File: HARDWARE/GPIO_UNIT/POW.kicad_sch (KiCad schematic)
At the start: 20 parts, among them J401 Screw_Terminal_01x02, U301 L78L05_SOT89, U901 MT2499A

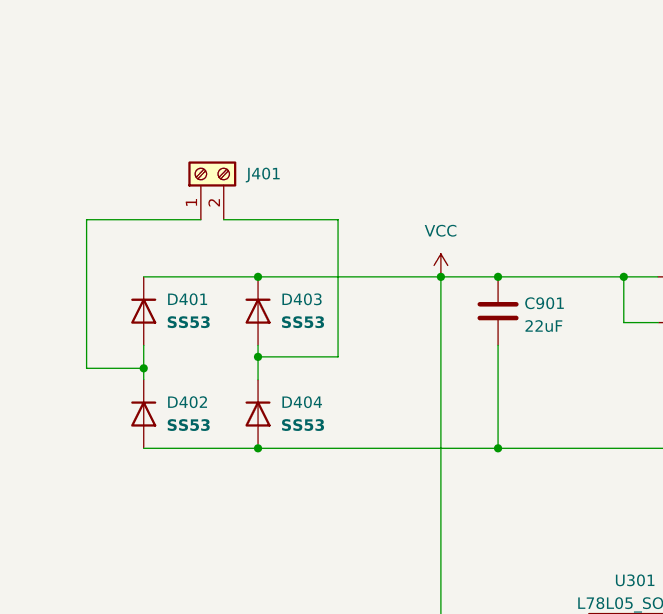
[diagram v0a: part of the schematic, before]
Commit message: added GPIO UNIT board. To be renamed Jack Of All trades
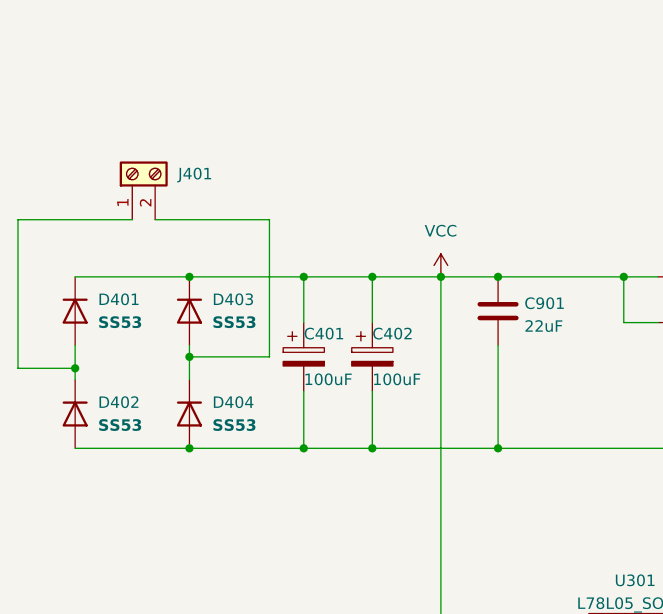
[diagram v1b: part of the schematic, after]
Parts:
- added C401, C402: 100uF, Capacitor_SMD:CP_Elec_6.3x5.8, symbol Device:C_Polarized
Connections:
- net GND: now also C401.2, C402.2
- net VCC: now also C401.1, C402.1
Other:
- moved on the sheet: D401, D402, D403, D404, J401
